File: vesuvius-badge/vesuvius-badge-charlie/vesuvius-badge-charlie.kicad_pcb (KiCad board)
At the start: 2 copper layers, 161.6 x 89 mm, 154 parts, among them U1 IS31FL3731-QF, U2 Pico

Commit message: letters done, now the rest of the wiring
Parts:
- added J1: Conn_01x06, Connector_PinHeader_2.54mm:PinHeader_1x06_P2.54mm_Horizontal, B.Cu at (152.4, 66.7)
- added J2: Conn_01x02, Connector_PinHeader_2.54mm:PinHeader_1x02_P2.54mm_Horizontal, B.Cu at (152.4, 85.7)
- C1, C3: footprint Capacitor_SMD:C_0603_1608Metric -> Capacitor_SMD:C_0402_1005Metric
- C2: value 10mF -> 10uF; footprint Capacitor_SMD:C_0603_1608Metric -> Capacitor_SMD:C_0402_1005Metric
- U2: footprint MCU_RaspberryPi_and_Boards:RPi_Pico_SMD_TH -> MCU_RaspberryPi_and_Boards:RPi_Pico_SMD
- moved U2 167.9 mm to (187.0, 96.2)
- moved U1 65.1 mm to (163.6, 79.8), turned to -90 degrees
- moved C3 63.0 mm to (163.6, 73.9), turned to 180 degrees
- moved C2 58.3 mm to (163.6, 72.2), turned to 180 degrees
- moved C1 57.2 mm to (163.6, 75.5), turned to 180 degrees
- moved R2 56.3 mm to (162.8, 46.7)
- moved R4 56.3 mm to (160.2, 54.2)
- moved R1 56.3 mm to (170.5, 47.7)
- moved R3 49.0 mm to (155.8, 43.5)
- moved D80 23.6 mm to (171.3, 70.9)
- moved D16 15.8 mm to (191.9, 75.8)
- moved D48 14.1 mm to (177.7, 75.6)
- moved D142 10.1 mm to (218.6, 80.5)
- moved D112 9.82 mm to (133.9, 82.5)
- moved D30 9.78 mm to (210.8, 73.2)
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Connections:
- net Net-(R3-Pad2) renamed I2C-AD
- U1 pad 3: unconnected-(U1-Pad3) -> VCC
- U1 pad 4: unconnected-(U1-Pad4) -> MCU_INTB
- U2 pad 20: unconnected-(U2-Pad20) -> MCU_INTB
- U2 pad 26: unconnected-(U2-Pad26) -> MCU_SDA
- U2 pad 27: unconnected-(U2-Pad27) -> MCU_SCL
- U2 pad 39: unconnected-(U2-Pad39) -> VCC
- U2 pad 40: VCC -> unconnected-(U2-Pad40)
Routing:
- net CA2: track 0.00 -> 32.2 mm, vias 0 -> 2
- net CA1: track 0.00 -> 30.6 mm, vias 0 -> 2
- net CA9: track 0.00 -> 24.6 mm
- net CA5: track 0.00 -> 19.9 mm
- net CA6: track 0.00 -> 19.6 mm
- net CA8: track 0.00 -> 12.7 mm
- net CA4: track 0.00 -> 12.5 mm, vias 0 -> 2
- net CA7: track 0.00 -> 9.99 mm
- net CA3: track 0.00 -> 9.73 mm
- net VCC: track 0.00 -> 5.77 mm
- net GND: track 0.00 -> 5.70 mm

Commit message: routing mostly dnoe
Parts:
- moved U2 72.9 mm to (199.4, 24.4)
- moved D64 8.74 mm to (145.4, 78.6), turned to 180 degrees
- moved D116 0.20 mm to (163.1, 110.0)
- turned D112 to 180 degrees
- turned D144 to 180 degrees
- turned D19 to 180 degrees
- turned D52 to 180 degrees
- turned D69 to 180 degrees
- turned D96 to 180 degrees
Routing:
- net CB9: track 0.00 -> 278.5 mm, vias 0 -> 6
- net CB7: track 0.00 -> 273.8 mm, vias 0 -> 15
- net CB6: track 0.00 -> 244.2 mm, vias 0 -> 16
- net CB8: track 0.00 -> 243.1 mm, vias 0 -> 18
- net CB4: track 0.00 -> 217.8 mm, vias 0 -> 15
- net CB5: track 0.00 -> 208.2 mm, vias 0 -> 13
- net CB3: track 0.00 -> 172.9 mm, vias 0 -> 18
- net CA9: track 24.6 -> 174.3 mm, vias 0 -> 6
- net CA8: track 12.7 -> 161.0 mm, vias 0 -> 15
- net CB2: track 0.00 -> 137.3 mm, vias 0 -> 13
- net CB1: track 0.00 -> 116.8 mm, vias 0 -> 4
- net CA7: track 9.99 -> 126.8 mm, vias 0 -> 12
- net CA6: track 19.6 -> 132.4 mm, vias 0 -> 14
- net CA5: track 19.9 -> 131.9 mm, vias 0 -> 10
- net CA4: track 12.5 -> 122.0 mm, vias 2 -> 14
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
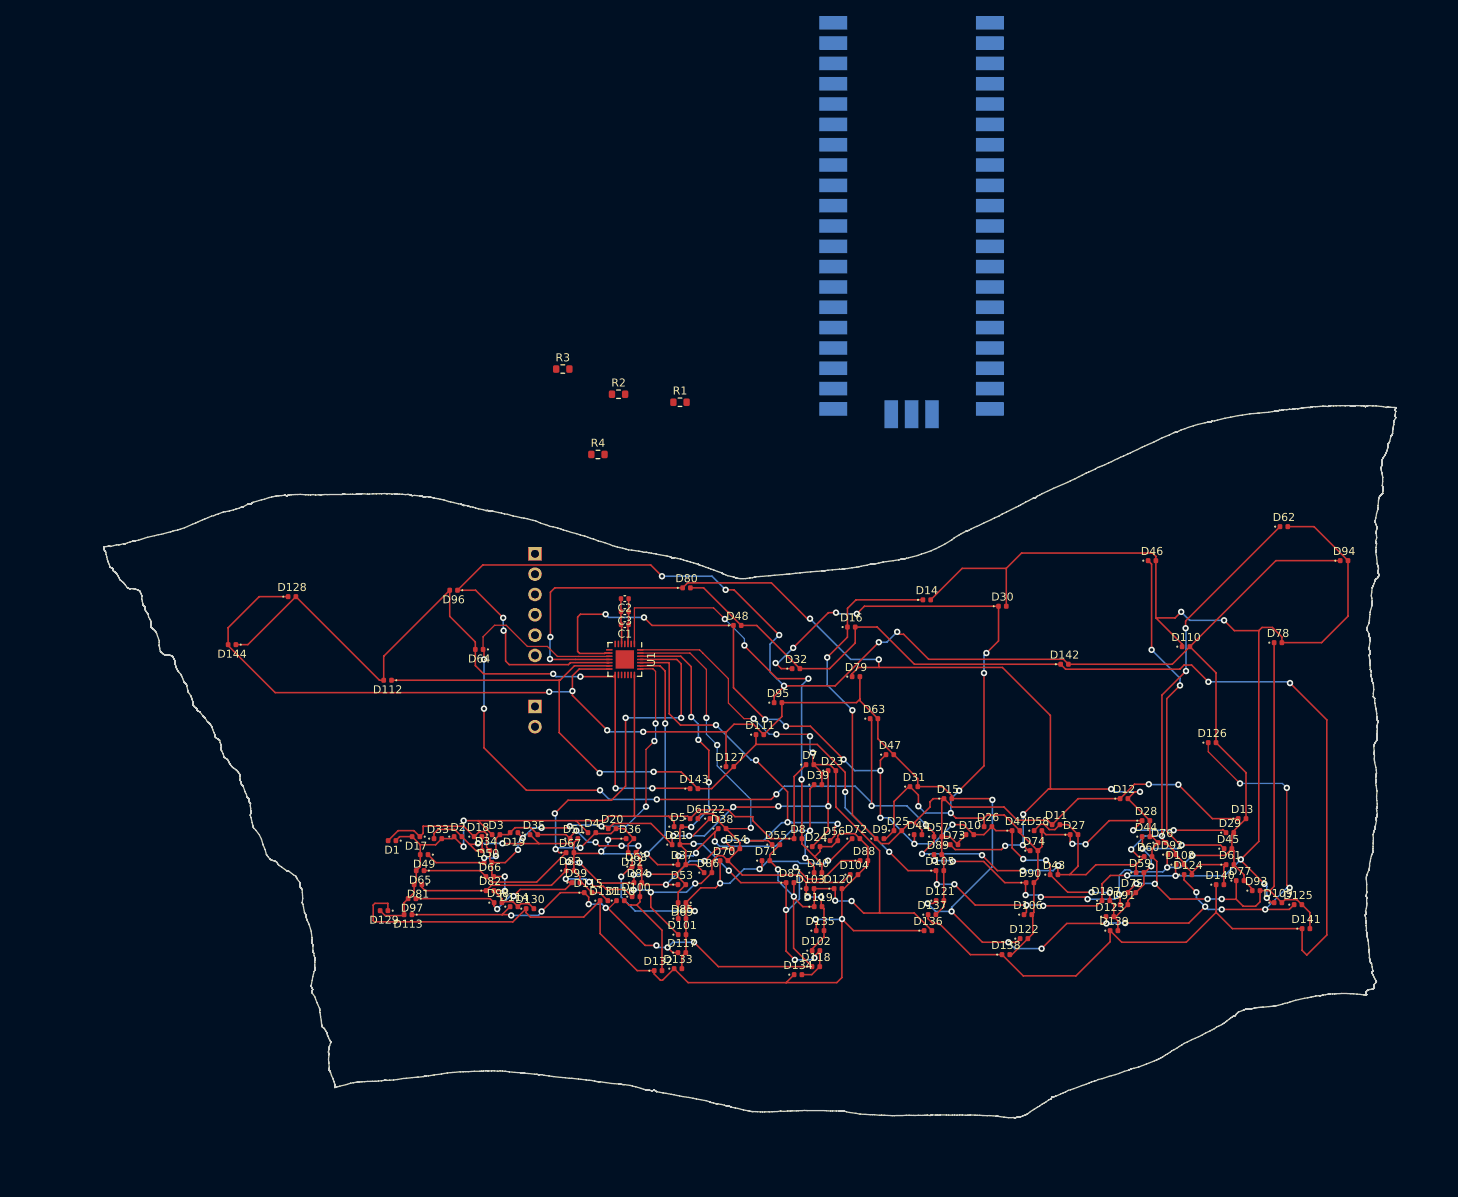
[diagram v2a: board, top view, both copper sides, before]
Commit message: wiring done
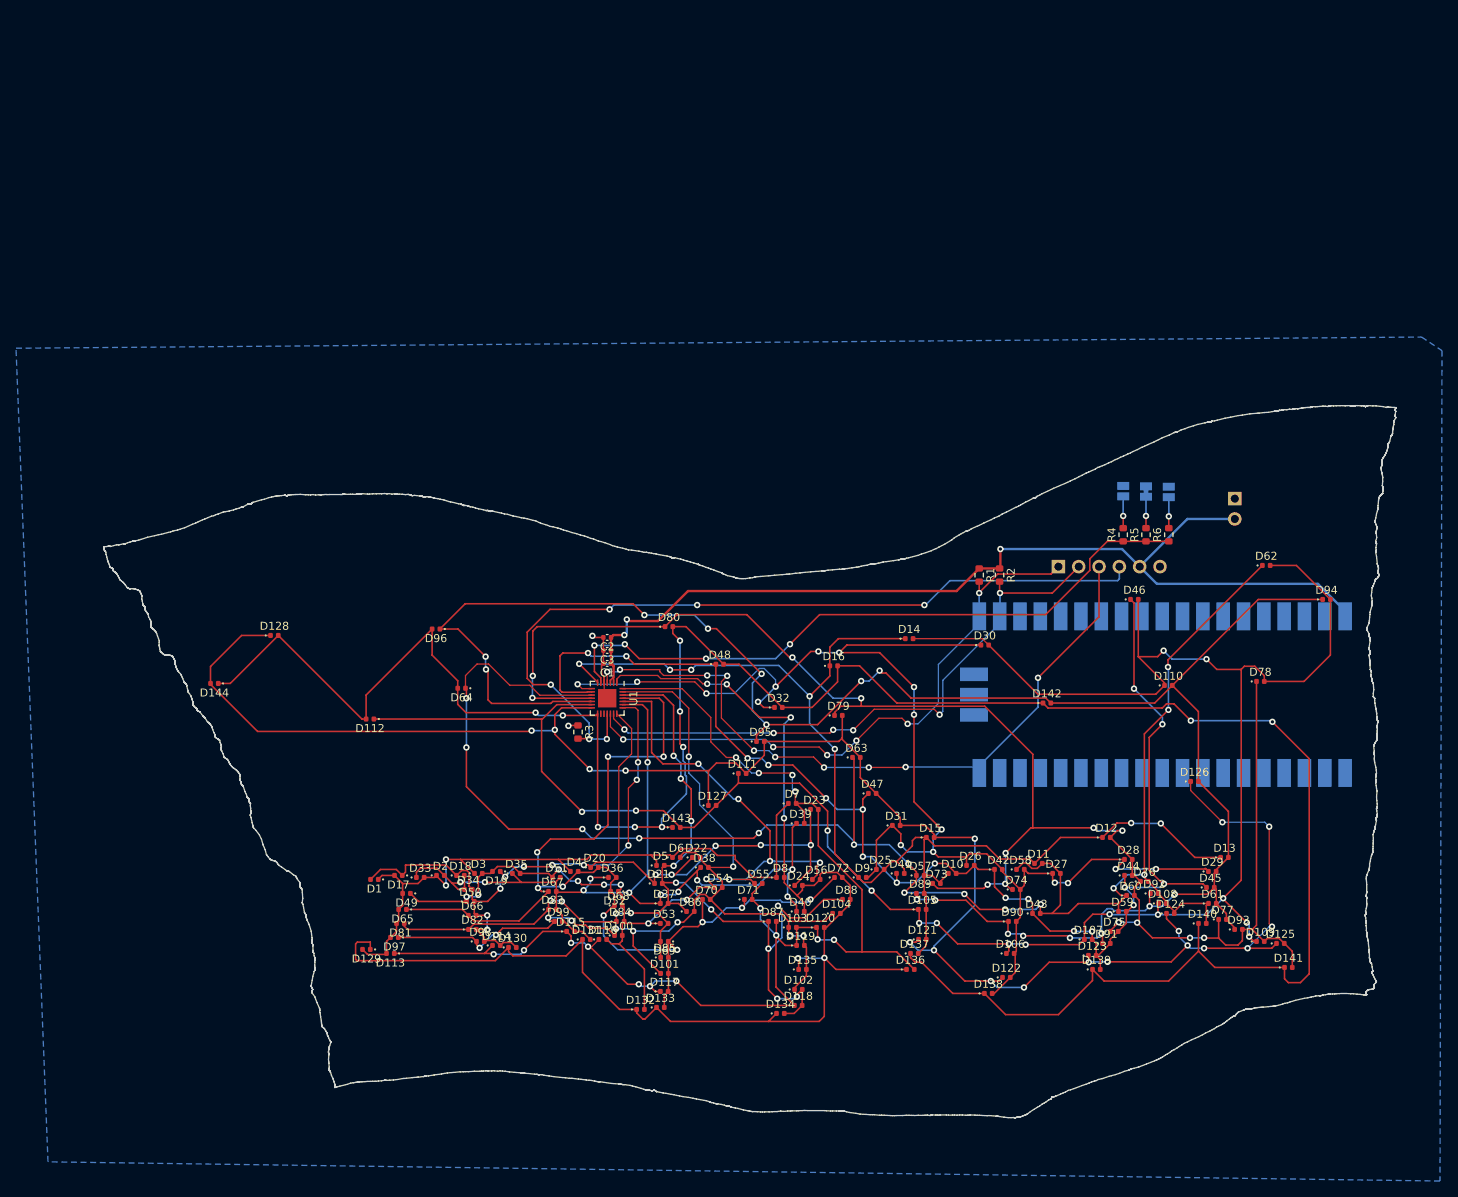
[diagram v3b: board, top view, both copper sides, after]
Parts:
- added JP1: SolderJumper_2_Open, Jumper:SolderJumper-2_P1.3mm_Open_Pad1.0x1.5mm, B.Cu at (225.9, 58.8)
- added JP2: SolderJumper_2_Bridged, Jumper:SolderJumper-2_P1.3mm_Bridged_Pad1.0x1.5mm, B.Cu at (228.8, 58.9)
- added JP3: SolderJumper_2_Open, Jumper:SolderJumper-2_P1.3mm_Open_Pad1.0x1.5mm, B.Cu at (231.6, 58.9)
- added R5: 16k, Resistor_SMD:R_0603_1608Metric, F.Cu at (228.8, 64.3)
- added R6: 20k, Resistor_SMD:R_0603_1608Metric, F.Cu at (231.6, 64.3)
- J1: footprint Connector_PinHeader_2.54mm:PinHeader_1x06_P2.54mm_Horizontal -> Connector_PinHeader_2.54mm:PinHeader_1x06_P2.54mm_Vertical
- J2: footprint Connector_PinHeader_2.54mm:PinHeader_1x02_P2.54mm_Horizontal -> Connector_PinHeader_2.54mm:PinHeader_1x02_P2.54mm_Vertical
- moved J2 91.3 mm to (239.8, 59.8)
- moved U2 68.2 mm to (232.1, 84.2), turned to 90 degrees
- moved R4 66.4 mm to (225.9, 64.3), turned to 90 degrees
- moved J1 65.4 mm to (217.8, 68.2), turned to -90 degrees
- moved R2 52.7 mm to (210.4, 69.3), turned to -90 degrees
- moved R3 45.4 mm to (157.8, 88.9), turned to -90 degrees
- moved R1 43.2 mm to (207.9, 69.3), turned to -90 degrees
- moved D64 5.33 mm to (143.2, 83.5)
- moved D16 5.33 mm to (189.7, 80.7)
- moved D48 5.33 mm to (175.5, 80.5)
- moved U1 5.33 mm to (161.4, 84.7)
- moved D10 5.33 mm to (204.5, 106.6)
- moved D105 5.33 mm to (200.8, 111.1)
- moved D106 5.33 mm to (211.8, 116.6)
- moved D107 5.33 mm to (221.5, 114.8)
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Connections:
- net Net-(R4-Pad1) renamed R_EXT
- R4 pad 2: GND -> Net-(R4-Pad2)
- U2 pad 13: unconnected-(U2-Pad13) -> GND
- U2 pad 18: unconnected-(U2-Pad18) -> GND
- U2 pad 21: unconnected-(U2-Pad21) -> MCU_SDA
- U2 pad 22: unconnected-(U2-Pad22) -> MCU_SCL
- U2 pad 23: unconnected-(U2-Pad23) -> GND
- U2 pad 26: MCU_SDA -> unconnected-(U2-Pad26)
- U2 pad 27: MCU_SCL -> unconnected-(U2-Pad27)
- U2 pad 28: unconnected-(U2-Pad28) -> GND
- U2 pad 3: unconnected-(U2-Pad3) -> GND
- U2 pad 38: unconnected-(U2-Pad38) -> GND
- U2 pad 42: GND -> unconnected-(U2-Pad42)
- U2 pad 8: unconnected-(U2-Pad8) -> GND
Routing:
- net VCC: track 5.77 -> 124.6 mm, vias 0 -> 3
- net I2C-AD: track 0.00 -> 103.0 mm, vias 0 -> 6
- net MCU_INTB: track 0.00 -> 88.5 mm, vias 0 -> 10
- net R_EXT: track 0.00 -> 84.5 mm, vias 0 -> 4
- net MCU_SDA: track 0.00 -> 75.9 mm, vias 0 -> 6
- net MCU_SCL: track 0.00 -> 74.6 mm, vias 0 -> 6
- net CB2: track 137.3 -> 172.8 mm, vias 13 -> 16
- net CB1: track 116.8 -> 151.1 mm, vias 4 -> 7
- net CB9: track 278.5 -> 303.6 mm, vias 6 -> 10
- net CA9: track 174.3 -> 168.4 mm
- net GND: track 5.70 -> 11.1 mm, vias 0 -> 2
- net Net-(R4-Pad2): track 0.00 -> 3.98 mm, vias 0 -> 1
- net Net-(JP2-Pad1): track 0.00 -> 3.92 mm, vias 0 -> 1
- net Net-(JP3-Pad1): track 0.00 -> 3.88 mm, vias 0 -> 1
- net CA1: track 103.9 -> 105.3 mm
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- added copper zone on B.Cu, net GND
